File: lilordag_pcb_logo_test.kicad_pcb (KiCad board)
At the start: 2 copper layers, 98.1 x 100 mm, 178 parts, among them J1 USB4105-GF-A, J2 826629-7, J3 826629-7, Q1 BC846, Q2 BC846, Q3 MMBT3906, Q4 MMBT3906, Q5 BC846, Q6 BC846, Q7 SSM3J56MFV, Q8 SSM3J56MFV, SW1 PCM12SMTR, SW2 PCM12SMTR, SW3 SW_MEC_5G, SW5 SW_MEC_5G, SW6 SW_MEC_5G, SW7 SW_MEC_5G, U1 ESP32-C3-MINI-1-N4, U2 WS2812B-B, U3 WS2812B-B, U4 WS2812B-B, U5 WS2812B-B

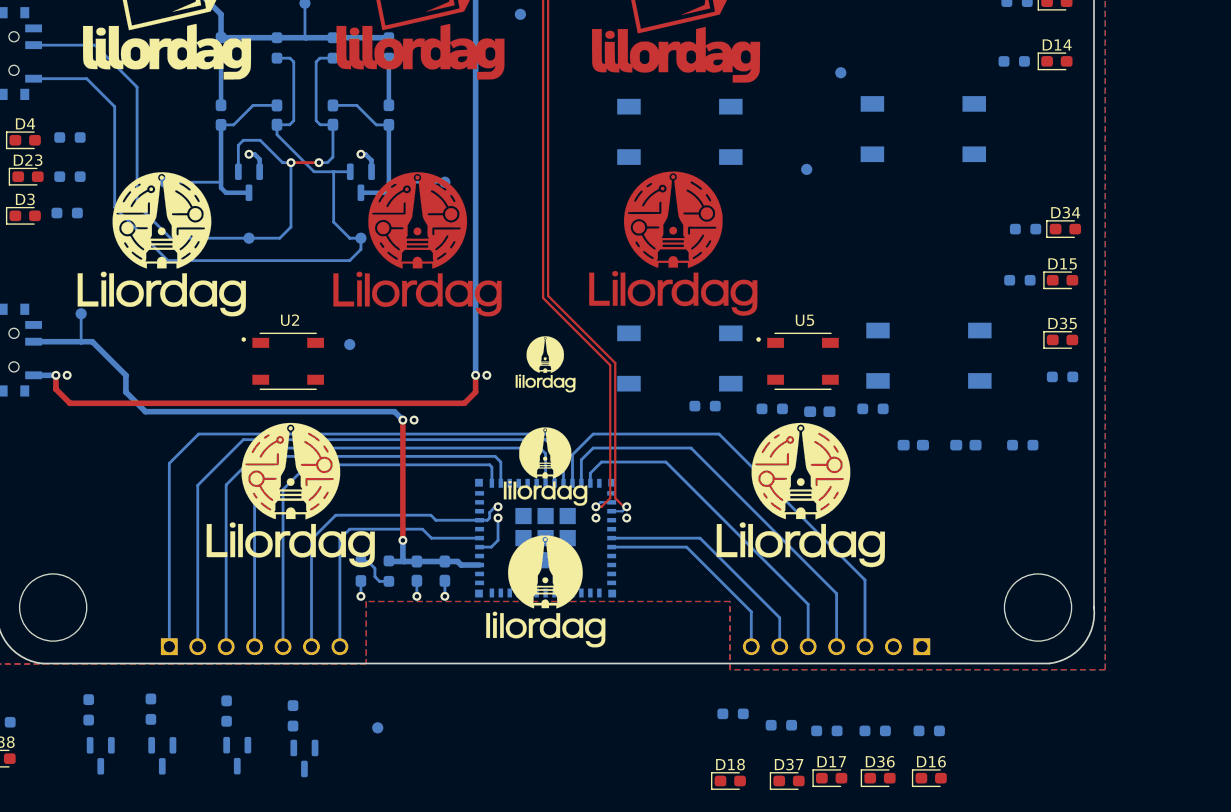
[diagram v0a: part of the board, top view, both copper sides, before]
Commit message: Buttons wired in
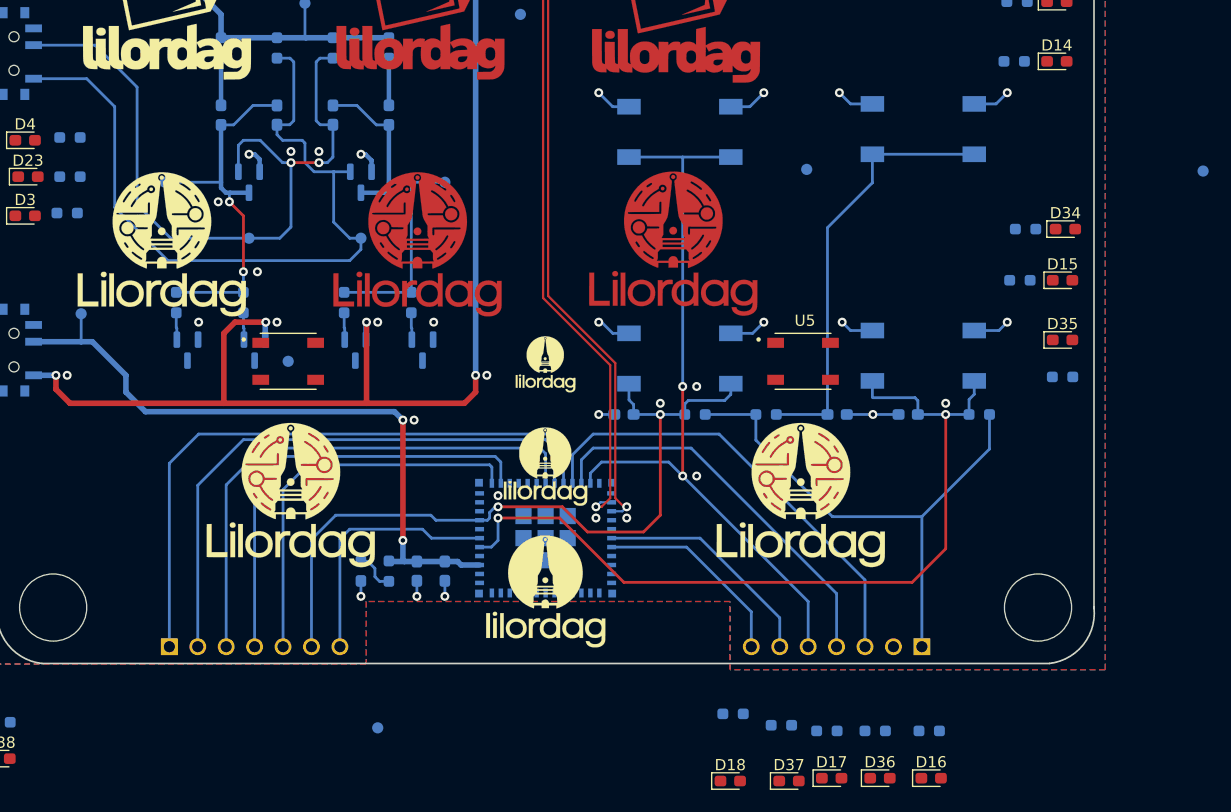
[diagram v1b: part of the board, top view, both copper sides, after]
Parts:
- removed the R55 at (91.2, 107.0)
- moved R10 38.4 mm to (65.0, 97.8)
- moved R31 38.0 mm to (59.0, 97.8)
- moved Q1 38.0 mm to (66.0, 102.0)
- moved Q3 37.7 mm to (60.0, 102.0)
- moved R33 37.3 mm to (50.0, 97.8)
- moved R12 37.2 mm to (44.0, 97.8)
- moved Q4 37.2 mm to (51.0, 102.0)
- moved Q2 37.1 mm to (45.0, 102.0)
- moved TP2 33.5 mm to (135.8, 86.0)
- moved R54 29.4 mm to (90.3, 107.8), turned to 0 degrees
- moved C5 26.0 mm to (84.0, 107.8)
- moved C9 11.8 mm to (103.0, 107.8), turned to 0 degrees
- moved R55 9.51 mm to (115.8, 107.8), turned to 0 degrees
- moved C8 7.90 mm to (109.4, 107.8)
- moved TP14 5.70 mm to (54.0, 103.0)
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- renumbered SW5 to BOOT, SW3 to ENABLE, SW6 to IO2, SW7 to IO8
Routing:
- net STRAP_IO2: track 3.90 -> 74.2 mm, vias 1 -> 2
- net V3.3-ESP: track 60.3 -> 108.0 mm
- net ENABLE: track 28.1 -> 67.0 mm, vias 1 -> 2
- net STRAP_IO8: track 35.5 -> 74.1 mm
- net BOOT: track 29.8 -> 67.6 mm, vias 0 -> 2
- net GND: track 8.59 -> 40.8 mm, vias 20 -> 43
- net +3.3V: track 145.7 -> 166.5 mm, vias 2 -> 4
- net LEFT_LED_CONNECTION: track 41.8 -> 57.7 mm
- net RIGHT_LED_CONNECTION: track 66.2 -> 81.7 mm, vias 0 -> 2
- net Net-(Q4-Pad1): track 0.00 -> 2.42 mm
- net Net-(Q2-Pad1): track 0.00 -> 2.42 mm
- net Net-(Q1-Pad1): track 0.00 -> 2.42 mm
- net Net-(Q3-Pad1): track 0.00 -> 2.42 mm
- net LEFT_BASE: track 67.5 -> 68.6 mm

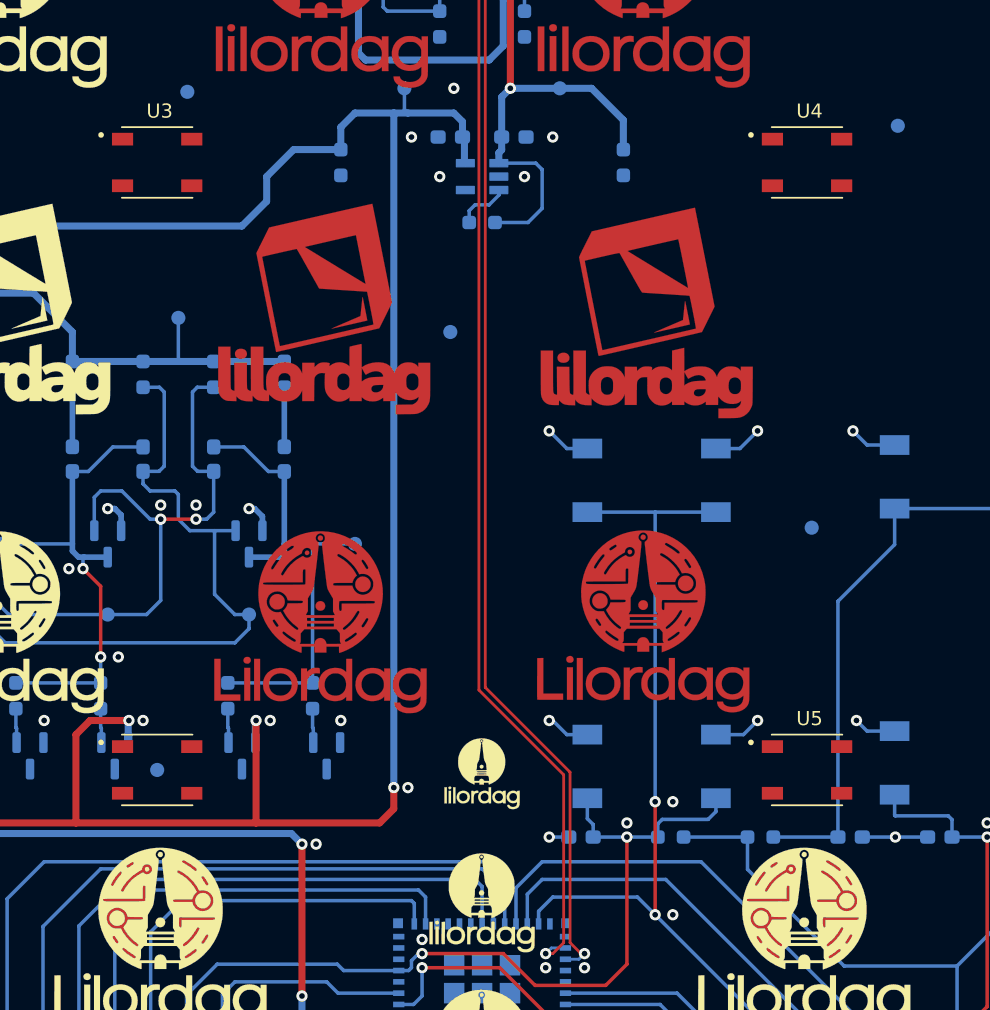
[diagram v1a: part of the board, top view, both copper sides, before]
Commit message: RGBs are wired in
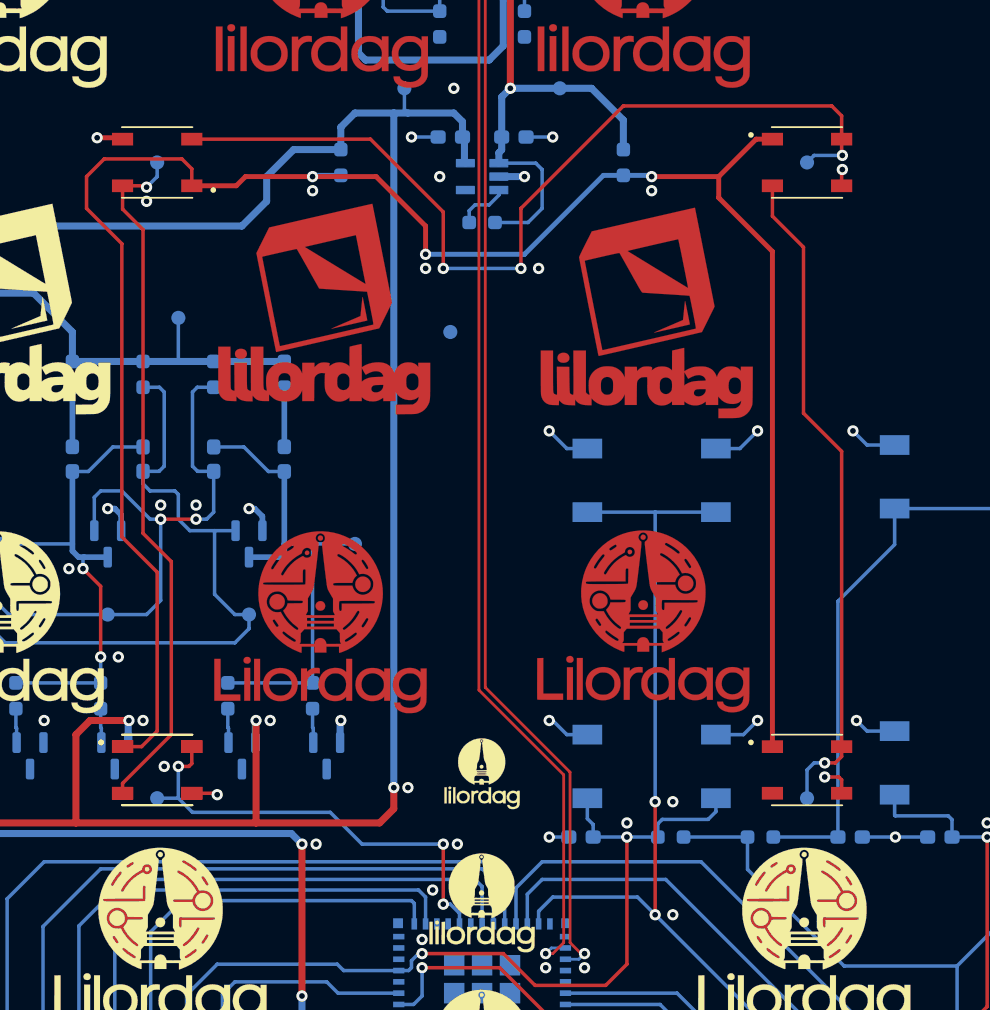
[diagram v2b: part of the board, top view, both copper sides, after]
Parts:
- added U2: WS2812B-B, WS2812B:LED_WS2812B-B, F.Cu at (54.0, 103.0)
- moved RGB3 19.2 mm to (100.0, 105.0)
- moved RGB2 6.93 mm to (100.0, 60.0)
- moved RGB1 5.44 mm to (54.0, 60.0)
- moved RGB0 2.00 mm to (54.0, 105.0)
- turned U3 to 180 degrees
- renumbered TP14 to RGB0, TP15 to RGB1, TP16 to RGB2, TP17 to RGB3
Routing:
- net Net-(R57-Pad1): track 0.00 -> 145.9 mm, vias 0 -> 3
- net Net-(TP16-Pad1): track 0.00 -> 65.2 mm, vias 0 -> 3
- net Net-(TP15-Pad1): track 0.00 -> 49.7 mm, vias 0 -> 1
- net Net-(TP17-Pad1): track 0.00 -> 47.3 mm, vias 0 -> 1
- net RGB: track 0.00 -> 32.5 mm, vias 0 -> 3
- net GND: track 40.8 -> 55.0 mm, vias 43 -> 55

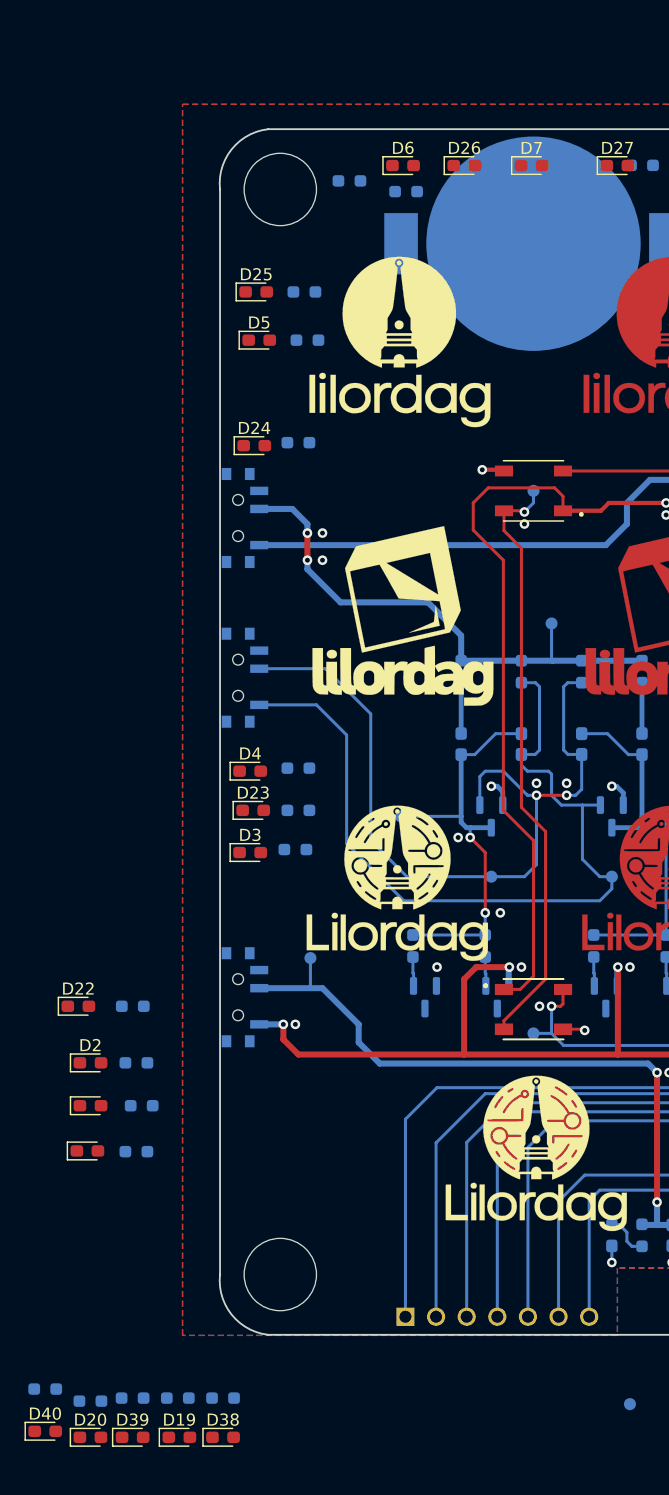
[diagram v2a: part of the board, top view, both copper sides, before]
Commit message: Arranding LEDs
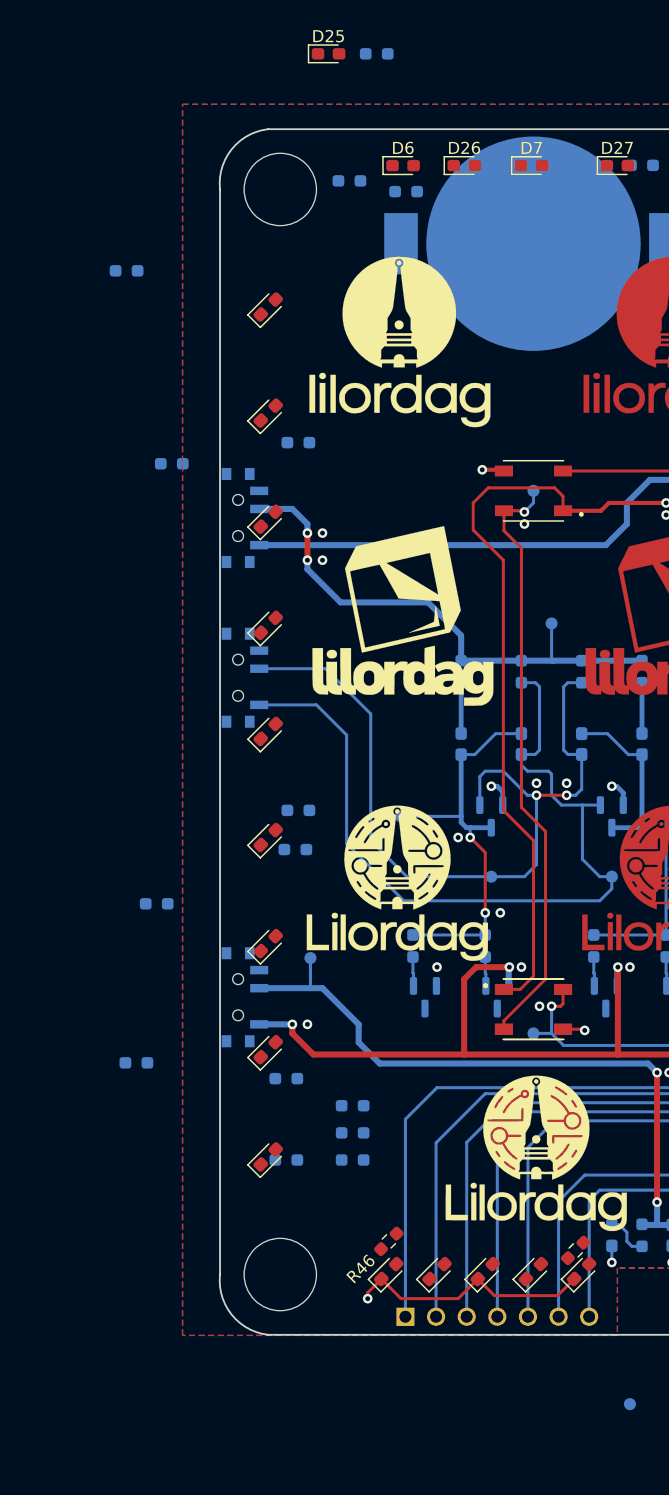
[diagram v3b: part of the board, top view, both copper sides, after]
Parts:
- R44, R46: moved to F.Cu
- moved D38 32.8 mm to (58.0, 124.8), turned to 45 degrees
- moved D19 32.4 mm to (54.0, 124.8), turned to 45 degrees
- moved D39 32.3 mm to (50.0, 124.8), turned to 45 degrees
- moved D20 31.9 mm to (46.0, 124.8), turned to 45 degrees
- moved R44 31.7 mm to (57.5, 123.0), turned to -135 degrees
- moved D40 31.4 mm to (42.0, 124.8), turned to 45 degrees
- moved R46 31.0 mm to (42.0, 122.2), turned to -135 degrees
- moved R24 29.5 mm to (39.0, 115.5), turned to 0 degrees
- moved R45 28.6 mm to (39.0, 113.2), turned to 0 degrees
- moved R23 28.3 mm to (39.0, 111.0), turned to 0 degrees
- moved R6 27.3 mm to (24.0, 57.8)
- moved D22 21.1 mm to (32.0, 88.8), turned to 45 degrees
- moved D4 21.0 mm to (32.0, 62.4), turned to 45 degrees
- moved D25 20.6 mm to (37.0, 23.8)
- moved R29 20.6 mm to (41.0, 23.8)
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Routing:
- net GND: track 55.0 -> 75.6 mm, vias 55 -> 56

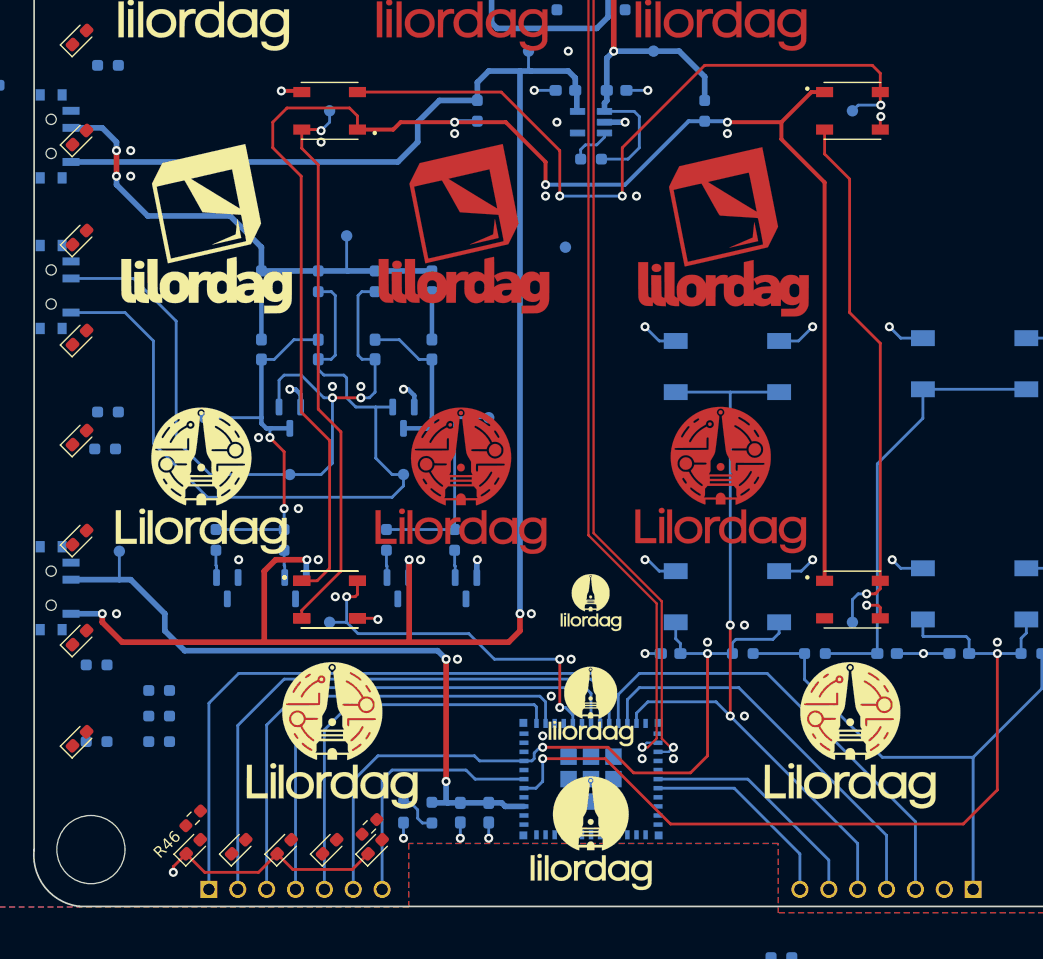
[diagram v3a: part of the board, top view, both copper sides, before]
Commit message: Bottom left LEDs arranged
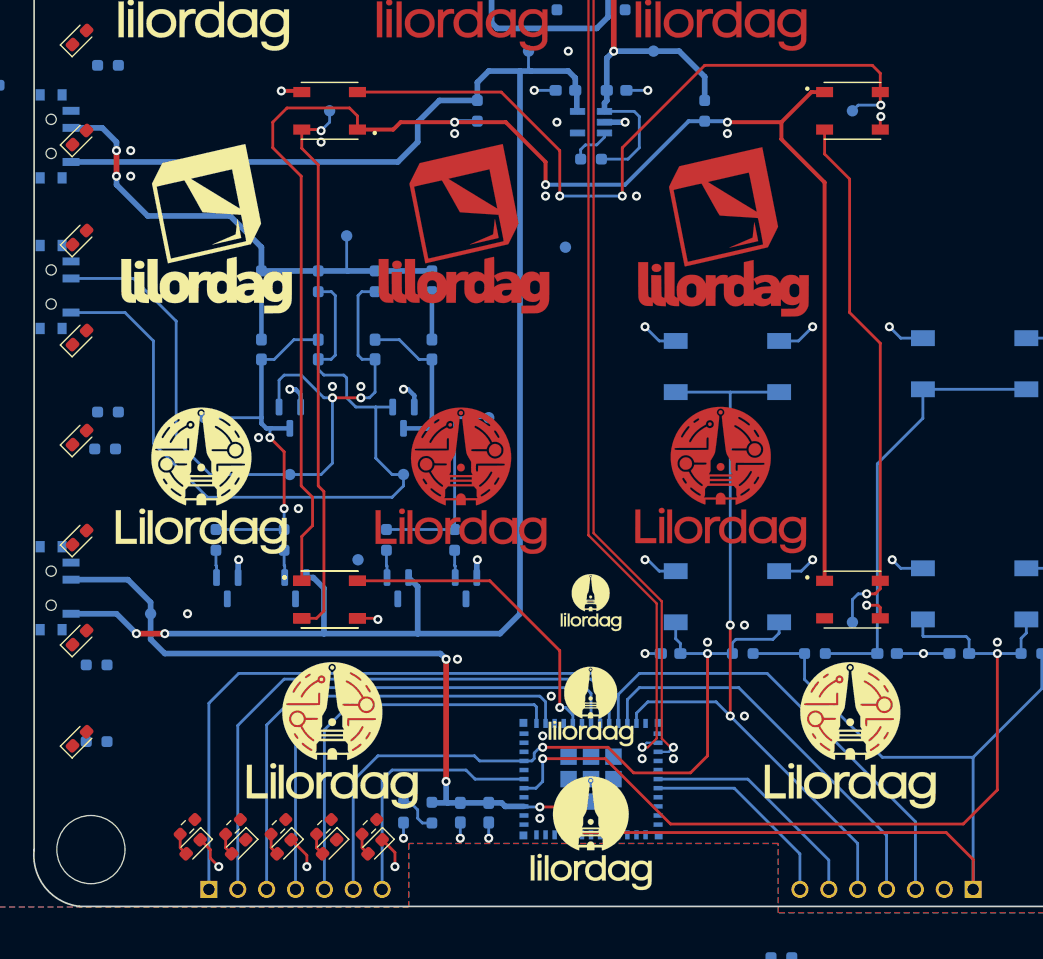
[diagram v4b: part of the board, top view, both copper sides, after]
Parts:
- R23, R24, R45: moved to F.Cu
- moved R23 18.8 mm to (53.5, 123.0), turned to -135 degrees
- moved R45 14.3 mm to (49.5, 123.0), turned to -135 degrees
- moved R24 9.92 mm to (45.5, 123.0), turned to -135 degrees
- moved ESP 3.3 6.15 mm to (38.2, 104.2)
- moved RGB0 6.04 mm to (56.5, 99.5)
- moved R46 0.90 mm to (41.5, 123.0)
- turned D19 to -135 degrees
- turned D20 to -135 degrees
- turned D38 to -135 degrees
- turned D39 to -135 degrees
- turned D40 to -135 degrees
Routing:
- net V3.3-ESP: track 108.0 -> 150.6 mm, vias 2 -> 3
- net +3.3V: track 166.2 -> 154.7 mm, vias 4 -> 2
- net GND: track 75.6 -> 65.5 mm, vias 56 -> 54
- net RGB: track 32.5 -> 27.5 mm, vias 3 -> 1
- net Net-(R57-Pad1): track 145.9 -> 143.9 mm
- net Net-(D40-Pad2): track 0.00 -> 1.94 mm
- net Net-(D39-Pad2): track 0.00 -> 1.94 mm
- net Net-(D38-Pad2): track 0.00 -> 1.94 mm
- net Net-(D20-Pad2): track 0.00 -> 1.94 mm
- net Net-(D19-Pad2): track 0.00 -> 1.94 mm
